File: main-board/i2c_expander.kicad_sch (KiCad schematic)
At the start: 2 parts, among them U21 TCA9548ARGER, U22 TCA9548ARGER

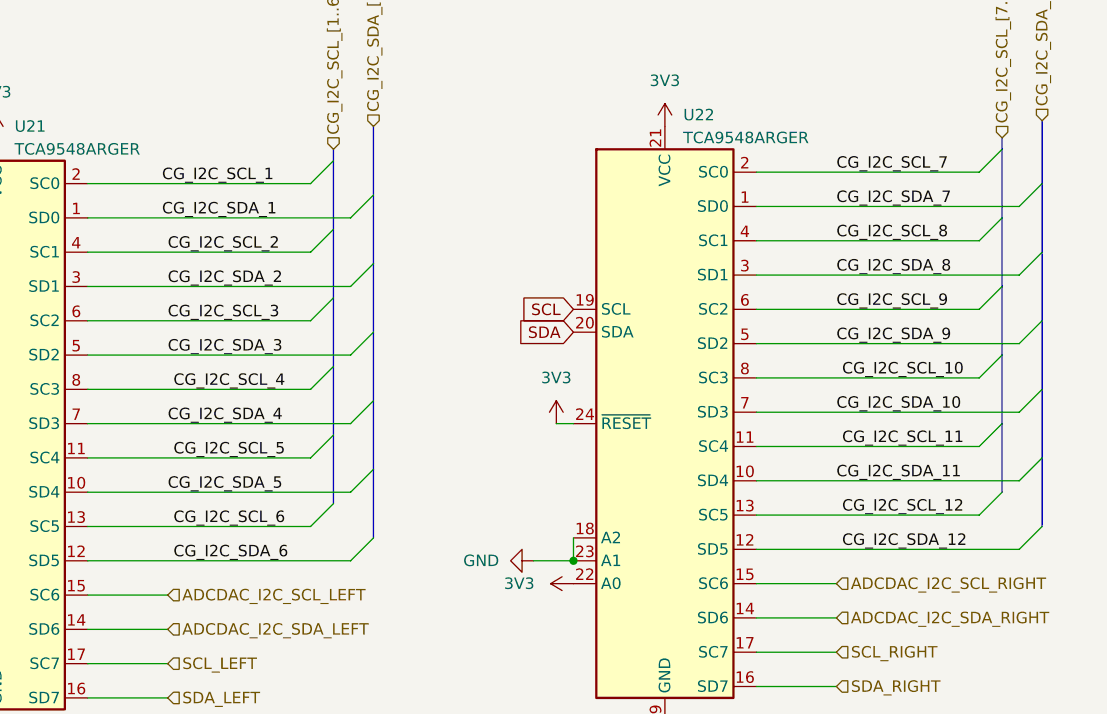
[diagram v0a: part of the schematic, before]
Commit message: Routed all power signals and re-organized GPIOs
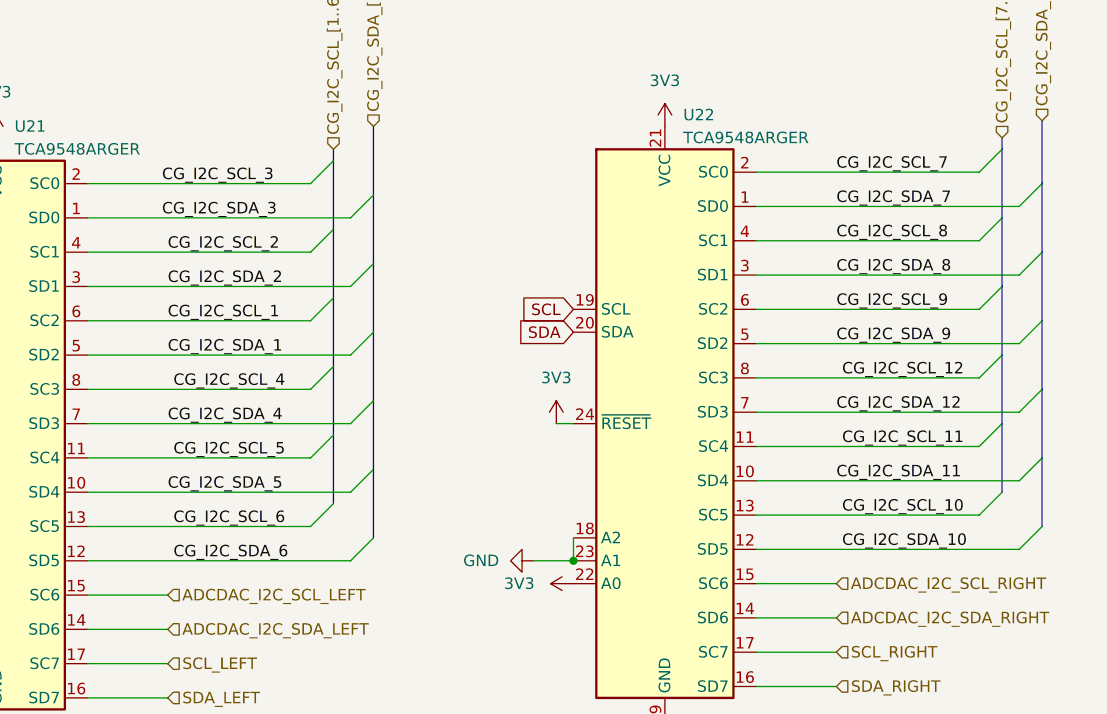
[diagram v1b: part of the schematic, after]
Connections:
- net CG_I2C_SCL_1: now also U21.6 (SC2); no longer U21.2 (SC0)
- net CG_I2C_SCL_10: now also U22.13 (SC5); no longer U22.8 (SC3)
- net CG_I2C_SCL_12: now also U22.8 (SC3); no longer U22.13 (SC5)
- net CG_I2C_SCL_3: now also U21.2 (SC0); no longer U21.6 (SC2)
- net CG_I2C_SDA_1: now also U21.5 (SD2); no longer U21.1 (SD0)
- net CG_I2C_SDA_10: now also U22.12 (SD5); no longer U22.7 (SD3)
- net CG_I2C_SDA_12: now also U22.7 (SD3); no longer U22.12 (SD5)
- net CG_I2C_SDA_3: now also U21.1 (SD0); no longer U21.5 (SD2)
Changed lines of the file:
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@@
 		)
 	)
-	(label "CG_I2C_SDA_3"
+	(label "CG_I2C_SDA_1"
 		(at 136.525 92.71 0)
 		(effects
@@
 		)
 	)
-	(label "CG_I2C_SDA_10"
+	(label "CG_I2C_SDA_12"
 		(at 210.82 99.06 0)
 		(effects
@@
 		)
 	)
-	(label "CG_I2C_SCL_10"
+	(label "CG_I2C_SCL_12"
 		(at 211.455 95.25 0)
 		(effects
@@
 		)
 	)
-	(label "CG_I2C_SDA_12"
+	(label "CG_I2C_SDA_10"
 		(at 211.455 114.3 0)
 		(effects
@@
 		)
 	)
-	(label "CG_I2C_SDA_1"
+	(label "CG_I2C_SDA_3"
 		(at 135.89 77.47 0)
 		(effects
@@
 		)
 	)
-	(label "CG_I2C_SCL_12"
+	(label "CG_I2C_SCL_10"
 		(at 211.455 110.49 0)
 		(effects
@@
 		)
 	)
-	(label "CG_I2C_SCL_1"
+	(label "CG_I2C_SCL_3"
 		(at 135.89 73.66 0)
 		(effects
@@
 		)
 	)
-	(label "CG_I2C_SCL_3"
+	(label "CG_I2C_SCL_1"
 		(at 136.525 88.9 0)
 		(effects

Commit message: pcb update
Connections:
- net ADCDAC_I2C_SCL_LEFT renamed SCL_CHEEP
- net ADCDAC_I2C_SCL_RIGHT: no longer names the net of U22.15 (SC6)
- net ADCDAC_I2C_SDA_LEFT renamed SDA_CHEEP
- net ADCDAC_I2C_SDA_RIGHT: no longer names the net of U22.14 (SD6)
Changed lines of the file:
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@@
 	(wire
 		(pts
-			(xy 127.635 123.19) (xy 136.525 123.19)
+			(xy 127.635 123.19) (xy 137.16 123.19)
 		)
 		(stroke
@@
 	(wire
 		(pts
-			(xy 127.635 119.38) (xy 136.525 119.38)
+			(xy 127.635 119.38) (xy 137.16 119.38)
 		)
 		(stroke
@@
 	(wire
 		(pts
-			(xy 127.635 127) (xy 136.525 127)
+			(xy 127.635 127) (xy 137.16 127)
 		)
 		(stroke
@@
 	(wire
 		(pts
-			(xy 127.635 130.81) (xy 136.525 130.81)
+			(xy 127.635 130.81) (xy 137.16 130.81)
 		)
 		(stroke
@@
 	(hierarchical_label "SCL_LEFT"
 		(shape input)
-		(at 136.525 127 0)
+		(at 137.16 127 0)
 		(effects
 			(font
@@
 		)
 	)
-	(hierarchical_label "ADCDAC_I2C_SCL_RIGHT"
-		(shape input)
-		(at 210.82 118.11 0)
+	(hierarchical_label "CG_I2C_SCL_[1..6]"
+		(shape input)
+		(at 154.94 69.85 90)
 		(effects
 			(font
@@
 		)
 	)
-	(hierarchical_label "CG_I2C_SCL_[1..6]"
-		(shape input)
-		(at 154.94 69.85 90)
+	(hierarchical_label "CG_I2C_SCL_[7..12]"
+		(shape input)
+		(at 229.235 68.58 90)
 		(effects
 			(font
@@
 		)
 	)
-	(hierarchical_label "CG_I2C_SCL_[7..12]"
-		(shape input)
-		(at 229.235 68.58 90)
+	(hierarchical_label "SCL_CHEEP"
+		(shape input)
+		(at 137.16 119.38 0)
 		(effects
 			(font
@@
 		)
 	)
-	(hierarchical_label "ADCDAC_I2C_SDA_RIGHT"
-		(shape input)
-		(at 210.82 121.92 0)
+	(hierarchical_label "SDA_LEFT"
+		(shape input)
+		(at 137.16 130.81 0)
 		(effects
 			(font
@@
 		)
 	)
-	(hierarchical_label "ADCDAC_I2C_SCL_LEFT"
-		(shape input)
-		(at 136.525 119.38 0)
+	(hierarchical_label "CG_I2C_SDA_[1..6]"
+		(shape input)
+		(at 159.385 67.31 90)
 		(effects
 			(font
@@
 		)
 	)
-	(hierarchical_label "SDA_LEFT"
-		(shape input)
-		(at 136.525 130.81 0)
+	(hierarchical_label "SCL_RIGHT"
+		(shape input)
+		(at 210.82 125.73 0)
 		(effects
 			(font
@@
 		)
 	)
-	(hierarchical_label "CG_I2C_SDA_[1..6]"
-		(shape input)
-		(at 159.385 67.31 90)
-		(effects
-			(font
-				(size 1.27 1.27)
-			)
-			(justify left)
-		)
-	)
-	(hierarchical_label "SCL_RIGHT"
-		(shape input)
-		(at 210.82 125.73 0)
-		(effects
-			(font
-				(size 1.27 1.27)
-			)
-			(justify left)
-		)
-	)
-	(hierarchical_label "ADCDAC_I2C_SDA_LEFT"
-		(shape input)
-		(at 136.525 123.19 0)
-		(effects
-			(font
+	(hierarchical_label "SDA_CHEEP"
+		(shape input)
+		(at 137.16 123.19 0)
+		(effects
+			(font

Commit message: PCB update
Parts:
- added J3: Conn_01x04, Connector_PinSocket_2.54mm:PinSocket_1x04_P2.54mm_Vertical, symbol Connector_Generic:Conn_01x04
- added R100, R101, R102, R103, R104, R105, R106, R107, R108, R109, R110, R12, R13, R80, R81, R82, R83, R85, R86, R87, R88, R89, R90, R91, R92, R93, R94, R97, R98, R99: 10k, Resistor_SMD:R_0603_1608Metric, symbol Device:R_Small
- U21, U22: LCSC (none) -> C555456
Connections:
- net 3V3: now also J3.4 (Pin_4), R100.1, R101.1, R102.1, R103.1, R104.1, R105.1, R106.1, R107.1, R108.1, R109.1, R110.1, R12.1, R13.1, R80.1, R81.1, R82.1, R83.1, R85.1, R86.1, R87.1, R88.1, R89.1, R90.1, R91.1, R92.1, R93.1, R94.1, R97.1, R98.1, R99.1
- net CG_I2C_SCL_1: now also R90.2
- net CG_I2C_SCL_10: now also R100.2
- net CG_I2C_SCL_11: now also R102.2
- net CG_I2C_SCL_12: now also R104.2
- net CG_I2C_SCL_2: now also R92.2
- net CG_I2C_SCL_3: now also R94.2
- net CG_I2C_SCL_4: now also R88.2
- net CG_I2C_SCL_5: now also R86.2
- net CG_I2C_SCL_6: now also R81.2
- net CG_I2C_SCL_7: now also R110.2
- net CG_I2C_SCL_8: now also R108.2
- net CG_I2C_SCL_9: now also R106.2
- net CG_I2C_SDA_1: now also R89.2
- net CG_I2C_SDA_10: now also R99.2
- net CG_I2C_SDA_11: now also R101.2
- net CG_I2C_SDA_12: now also R103.2
- net CG_I2C_SDA_2: now also R91.2
- net CG_I2C_SDA_3: now also R93.2
- net CG_I2C_SDA_4: now also R87.2
- net CG_I2C_SDA_5: now also R85.2
- net CG_I2C_SDA_6: now also R80.2
- net CG_I2C_SDA_7: now also R109.2
- net CG_I2C_SDA_8: now also R107.2
- net CG_I2C_SDA_9: now also R105.2
- net GND: now also J3.1 (Pin_1)
- net SCL_CHEEP: now also R13.2
- net SCL_LEFT: now also R83.2
- net SDA_CHEEP: now also R12.2
- net SDA_LEFT: now also R82.2
- net SDA_EXT: now reaches U22.14 (SD6)
- net SDA_EXT: now also J3.3 (Pin_3), R98.2
- net SCL_EXT: now reaches U22.15 (SC6)
- net SCL_EXT: now also J3.2 (Pin_2), R97.2
- net SCL_RIGHT: no longer names the net of U22.17 (SC7)
- net SDA_RIGHT: no longer names the net of U22.16 (SD7)
- no-connect marks 0 -> 2
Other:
- moved on the sheet: U21, U22

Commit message: Testing board final version & production data
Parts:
- added C35, C46, C47: 100nF, Capacitor_SMD:C_0603_1608Metric, symbol Device:C_Small
- added R26, R72: 10k, Resistor_SMD:R_0603_1608Metric, symbol Device:R_Small
- added U12: 24AA02E-OT, Package_TO_SOT_SMD:SOT-23-5, symbol Memory_EEPROM:24AA02E-OT
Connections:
- net 3V3: now also C35.1, C46.1, C47.1, R26.1, R72.1, U12.4 (V_{CC})
- net GND: now also C35.2, C46.2, C47.2, U12.2 (V_{SS})
- net SDA_EEPROM: now reaches U22.16 (SD7)
- net SDA_EEPROM: now also R26.2, U12.3 (SDA)
- net SCL_EEPROM: now reaches U22.17 (SC7)
- net SCL_EEPROM: now also R72.2, U12.1 (SCL)
- no-connect marks 2 -> 0

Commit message: production files
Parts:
- U12: LCSC (none) -> C38987
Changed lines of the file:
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@@
+			)
+		)
+		(property "LCSC" "C38987"
+			(at 143.51 161.2899 0)
+			(effects
+				(font
+					(size 1.27 1.27)
+				)
+				(hide yes)
 			)
 		)
